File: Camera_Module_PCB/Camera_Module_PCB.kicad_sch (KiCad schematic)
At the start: 56 parts, among them J3 FFC2A32-24-T, SW2 SW_Push, SW3 SW_Push, U2 ESP32-S3R8, U4 MAX98357AETE_T, Y1 40MHz

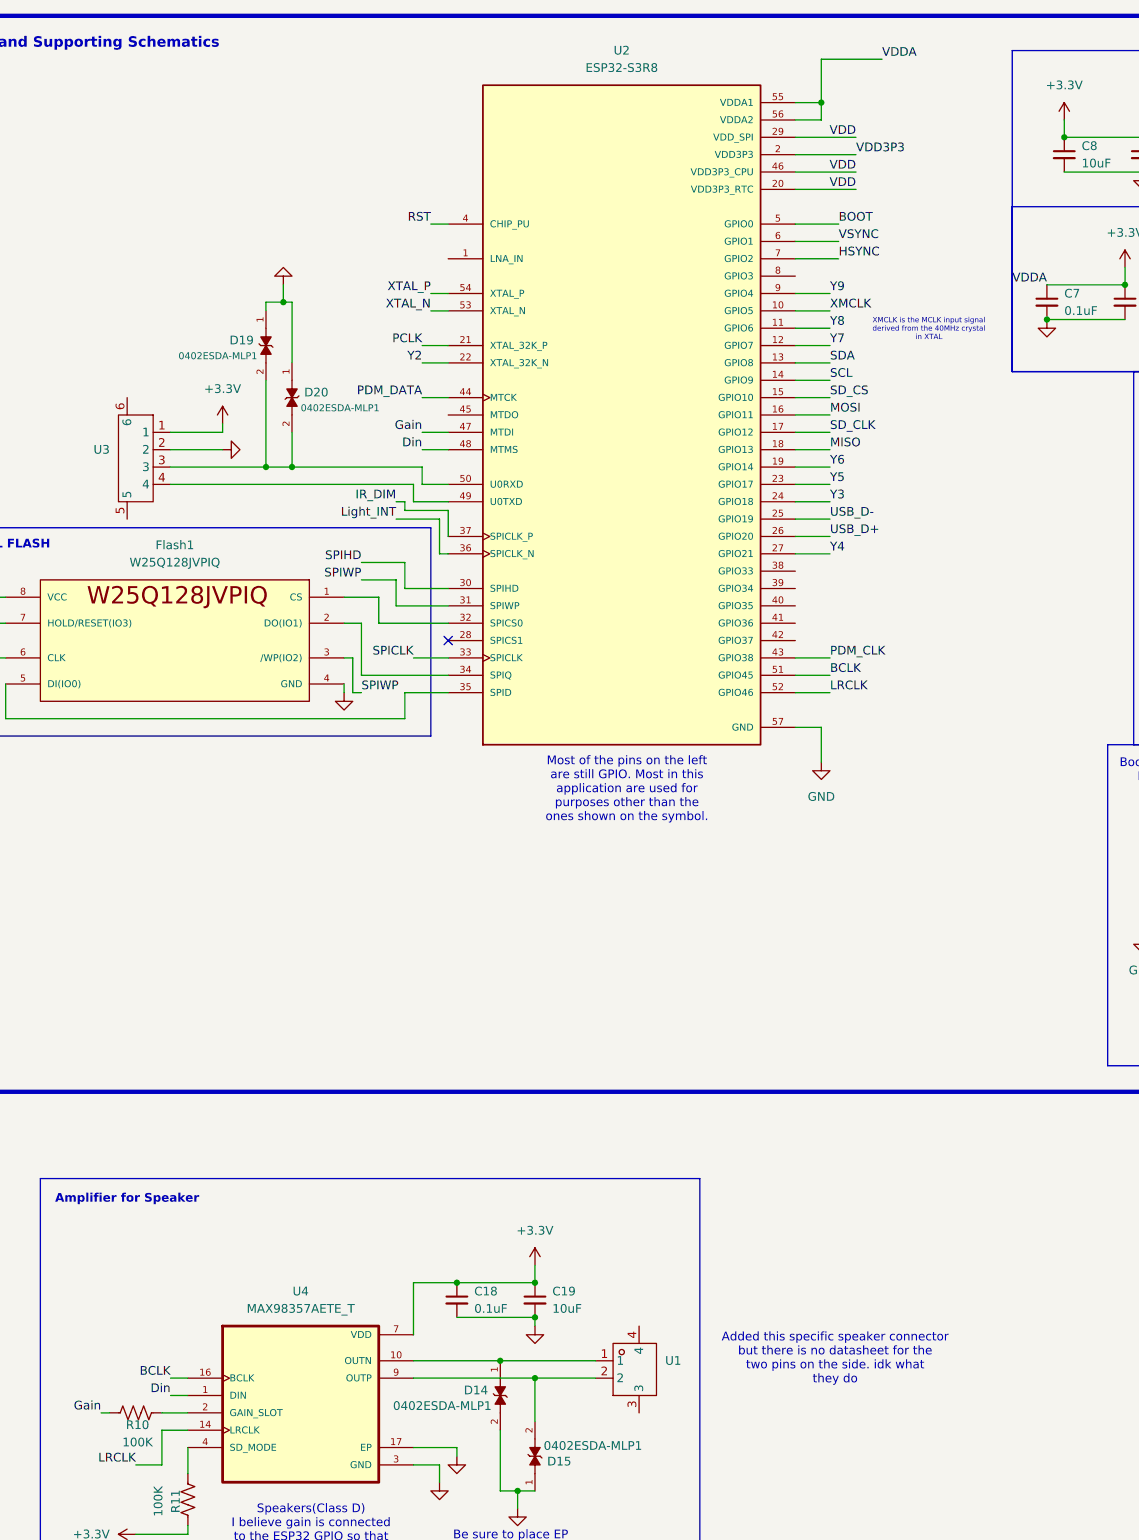
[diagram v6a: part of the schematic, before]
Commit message: Began early Layout for PCB
Moved most of the ICs into a general area layout for the PCB.
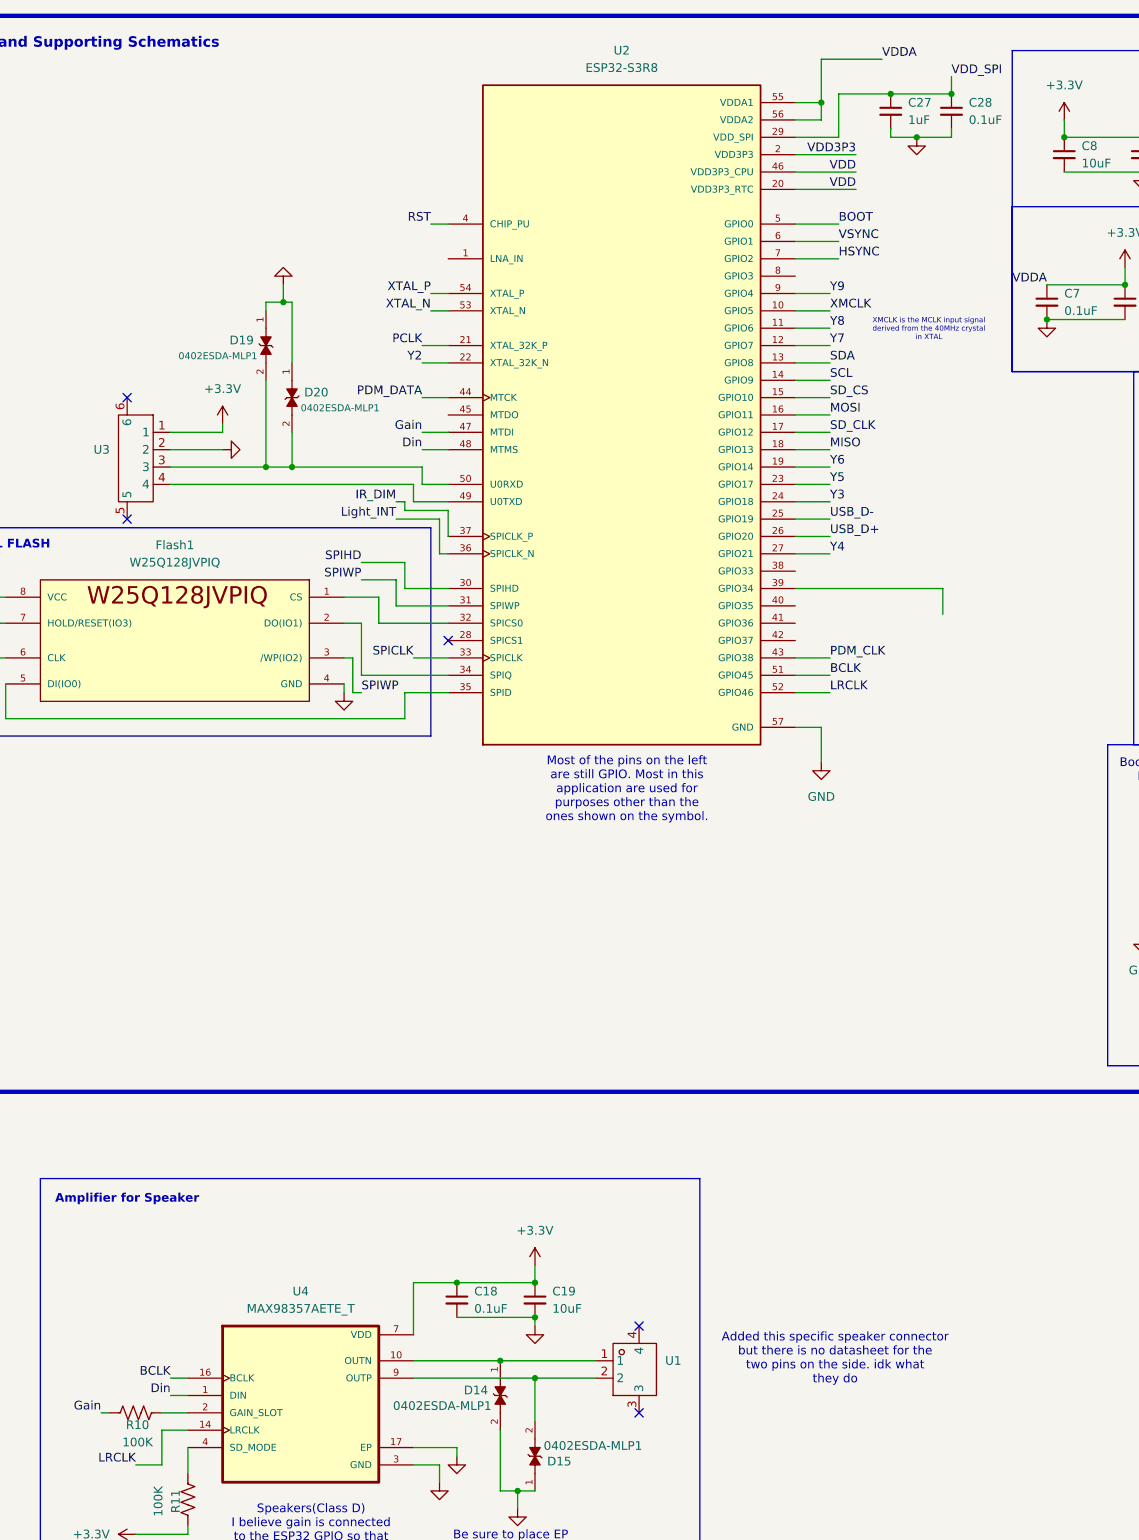
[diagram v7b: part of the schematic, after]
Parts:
- added C27: 1uF, Capacitor_SMD:C_0603_1608Metric, symbol Device:C_Small
- added C28: 0.1uF, Capacitor_SMD:C_0603_1608Metric, symbol Device:C_Small
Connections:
- net +3.3V: no longer U2.29 (VDD_SPI)
- net GND: now also C27.2, C28.2
- net VDD_SPI: now also U2.29 (VDD_SPI), C27.1, C28.1
- no-connect marks 7 -> 11

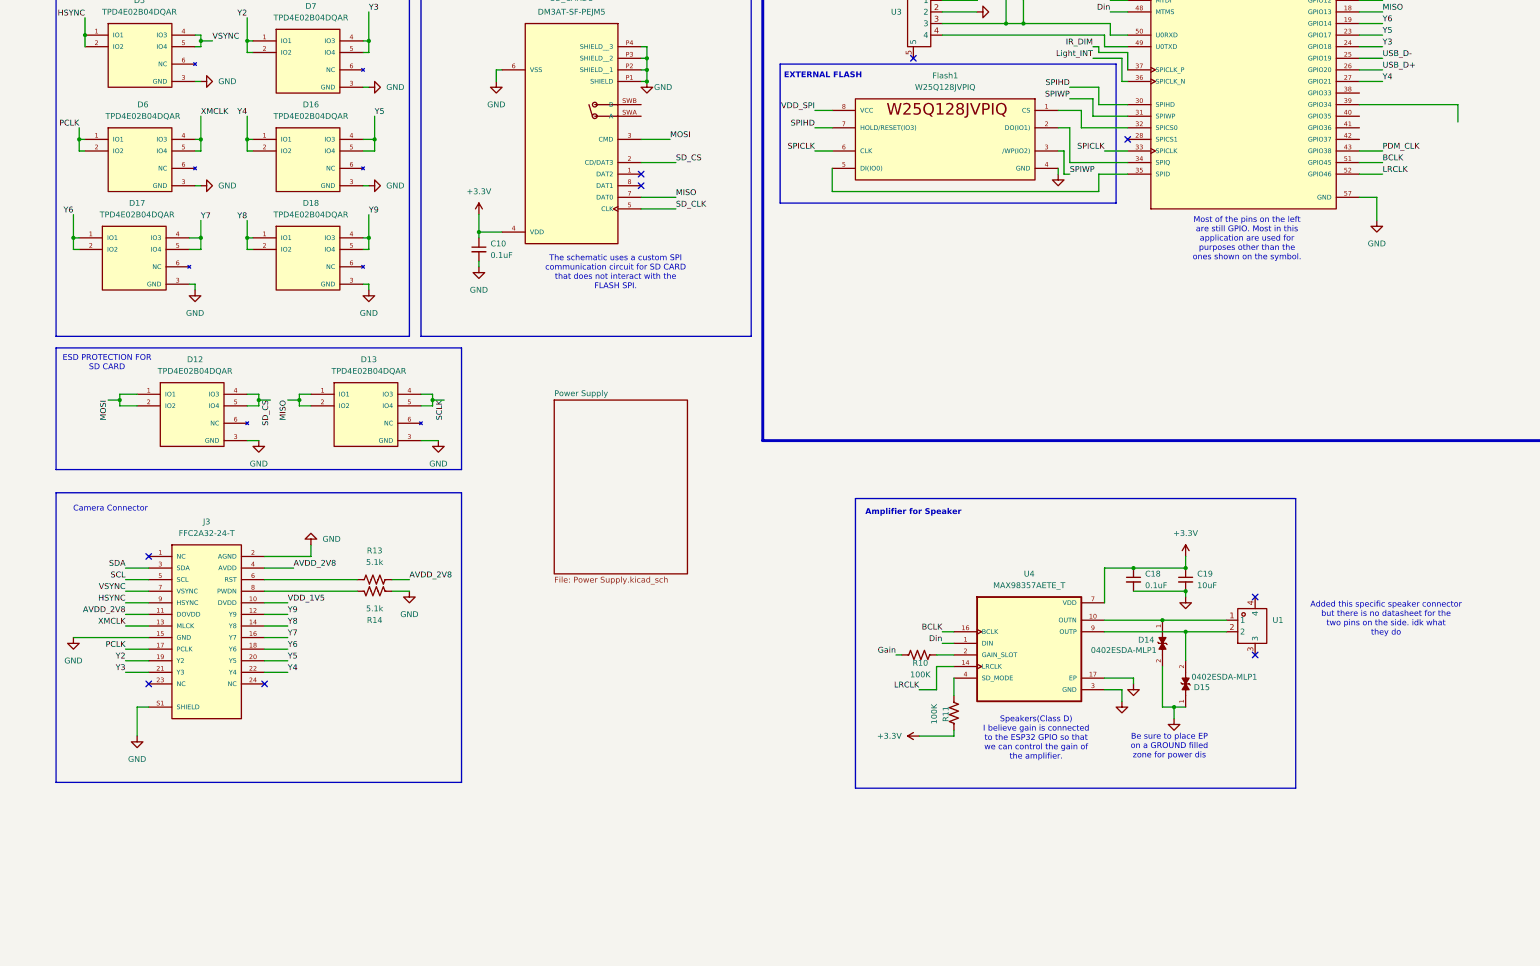
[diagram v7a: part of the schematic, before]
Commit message: Finished Schematic Except for a small few passives
Finished all of the connections in the schematic page and added a new LED driver. A small selection of passive elements must be given proper values after some calculations.
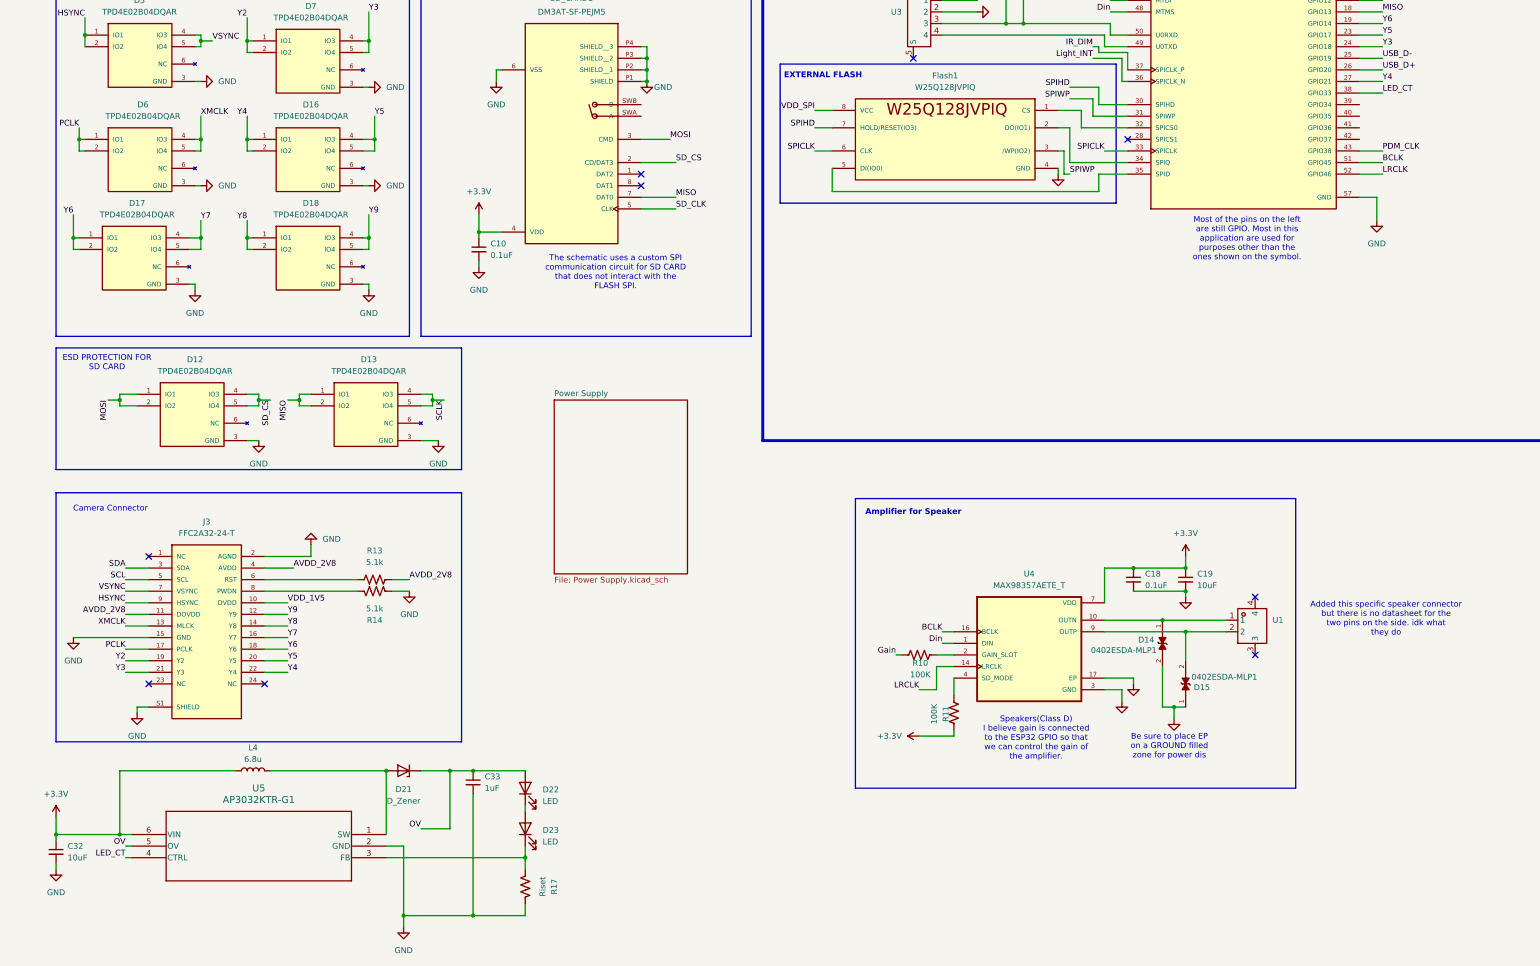
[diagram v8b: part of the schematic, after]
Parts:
- added C32: 10uF, Capacitor_SMD:C_0603_1608Metric, symbol Device:C_Small
- added C33: 1uF, Capacitor_SMD:C_0603_1608Metric, symbol Device:C_Small
- added D21: D_Zener, Diode_SMD:D_0603_1608Metric, symbol Device:D_Zener
- added D22, D23: LED, LED_SMD:LED_2010_5025Metric, symbol Device:LED
- added L4: 6.8u, Inductor_SMD:L_0603_1608Metric, symbol Device:L
- added R17: Riset, Resistor_SMD:R_0603_1608Metric, symbol Device:R_US
- added U5: AP3032KTR-G1, AP3032KTR-G1:SOT23-6_DIO, symbol AP3032KTR-G1:AP3032KTR-G1
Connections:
- net +3.3V: now also C32.1, L4.1, U5.6 (VIN)
- net GND: now also C32.2, C33.2, R17.2, U5.2 (GND)
- net LED_CT: now reaches U2.38 (GPIO33)
- net LED_CT: now also U5.4 (CTRL)
- new net: D23.1 (K), R17.1, U5.3 (FB)
- new net: D22.1 (K), D23.2 (A)
- new net: D21.2 (A), L4.2, U5.1 (SW)
- new net OV: C33.1, D21.1 (K), D22.2 (A), U5.5 (OV)
